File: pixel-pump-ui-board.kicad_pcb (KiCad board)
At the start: 4 copper layers, 36.4 x 49.3 mm, 48 parts, among them J1 SM10B-SRSS-TB, SW1 B3U-1000P, SW2 B3U-1000P, SW3 B3U-1000P, SW4 B3U-1000P, SW5 B3U-1000P, SW6 B3U-1000P, U1 WS2812B-2020, U10 WS2812B-2020, U11 WS2812B-2020, U12 WS2812B-2020, U2 WS2812B-2020, U3 WS2812B-2020, U4 WS2812B-2020, U5 WS2812B-2020, U6 WS2812B-2020, U7 WS2812B-2020, U8 WS2812B-2020, U9 WS2812B-2020

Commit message: Update appearance
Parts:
- moved kibuzzard-6108471A 1.08 mm to (81.6, 87.0)
- moved kibuzzard-61084704 1.08 mm to (81.8, 84.1)

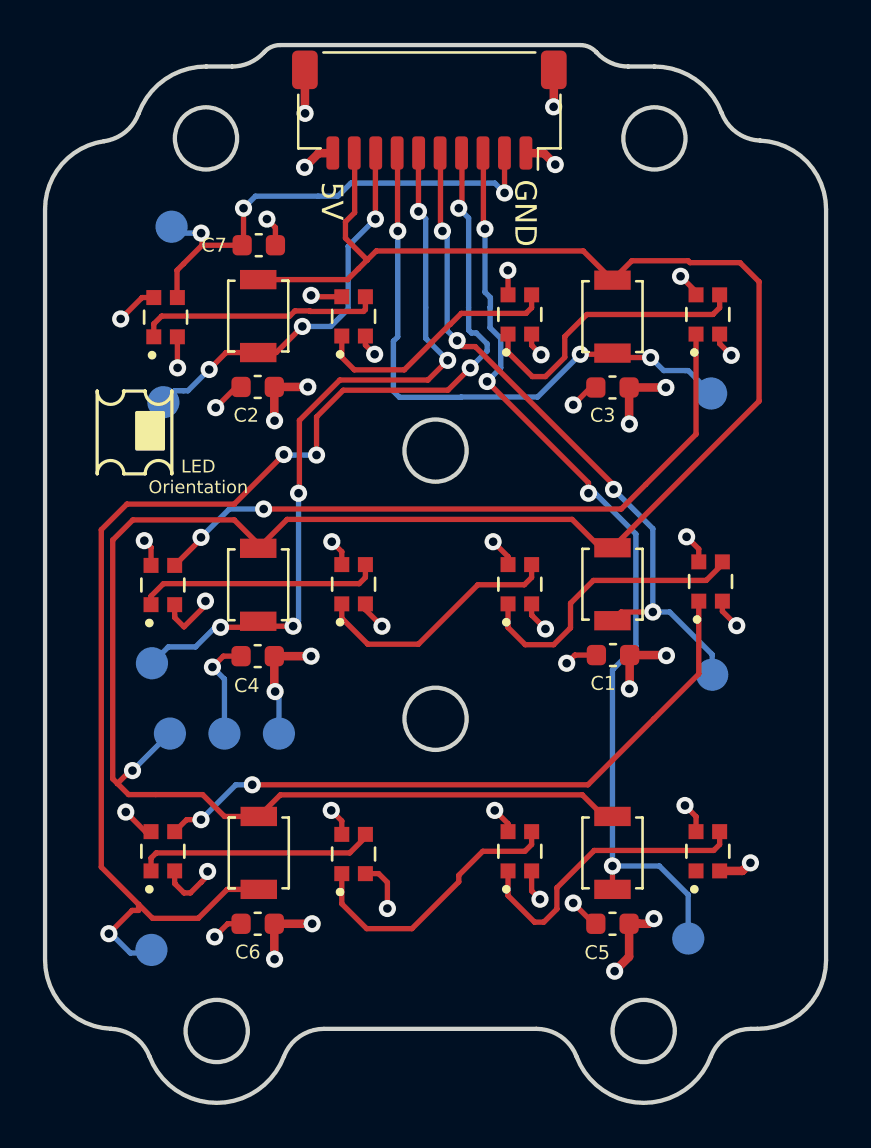
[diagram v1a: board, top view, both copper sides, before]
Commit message: Add fiducials and open mounting holes from 2.9 to 3.1 mm
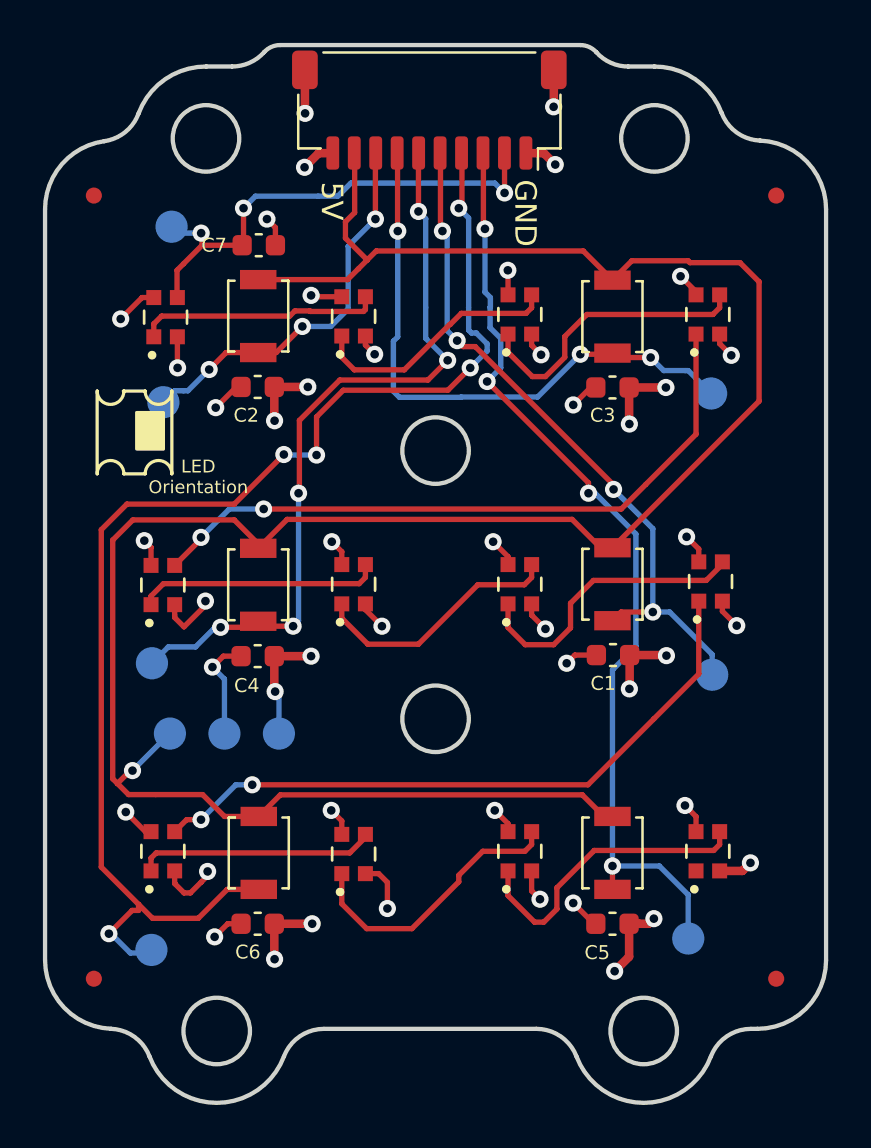
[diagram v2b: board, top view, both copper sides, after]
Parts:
- removed kibuzzard-61084595: G***, kibuzzard-61084595
- removed kibuzzard-610845E2: G***, kibuzzard-610845E2
- removed kibuzzard-610845ED: G***, kibuzzard-610845ED
- removed kibuzzard-6108460F: G***, kibuzzard-6108460F
- removed kibuzzard-61084618: G***, kibuzzard-61084618
- removed kibuzzard-6108463B: G***, kibuzzard-6108463B
- removed kibuzzard-61084660: G***, kibuzzard-61084660
- removed kibuzzard-61084691: G***, kibuzzard-61084691
- removed kibuzzard-610846A8: G***, kibuzzard-610846A8
- removed kibuzzard-610846B1: G***, kibuzzard-610846B1
- added FID1: Fiducial, Fiducial:Fiducial_0.75mm_Mask1.5mm, F.Cu at (66.0, 105.0)
- added FID2: Fiducial, Fiducial:Fiducial_0.75mm_Mask1.5mm, F.Cu at (66.0, 68.5)
- added FID3: Fiducial, Fiducial:Fiducial_0.75mm_Mask1.5mm, F.Cu at (97.8, 68.5)
- added FID4: Fiducial, Fiducial:Fiducial_0.75mm_Mask1.5mm, F.Cu at (97.8, 105.0)
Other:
- outline, holes or cut-outs redrawn
- board text added: "REV 5"
- board text removed: "REV 4"
